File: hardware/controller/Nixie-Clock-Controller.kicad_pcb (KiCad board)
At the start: 2 copper layers, 228.6 x 69.8 mm, 67 parts, among them IC1 ESP32-DEVKITC-V4, IC2 74141, J1 9/12-35V DC in, J2 Nixies-Connector, J3 Input, J4 Output, J5 LEDs, J6 power_out, Q1 MPSA42, Q10 MPSA42, Q11 MPSA42, Q12 MPSA42, Q13 MPSA42, Q14 MPSA42, Q2 MPSA92, Q3 MPSA92, Q4 MPSA92, Q5 MPSA92, Q6 MPSA92, Q7 MPSA92, Q8 MPSA92, Q9 MPSA42, SW1 on/off, SW2 in voltage select, U1 L7805, U2 L7809, U3 NCH6300HV

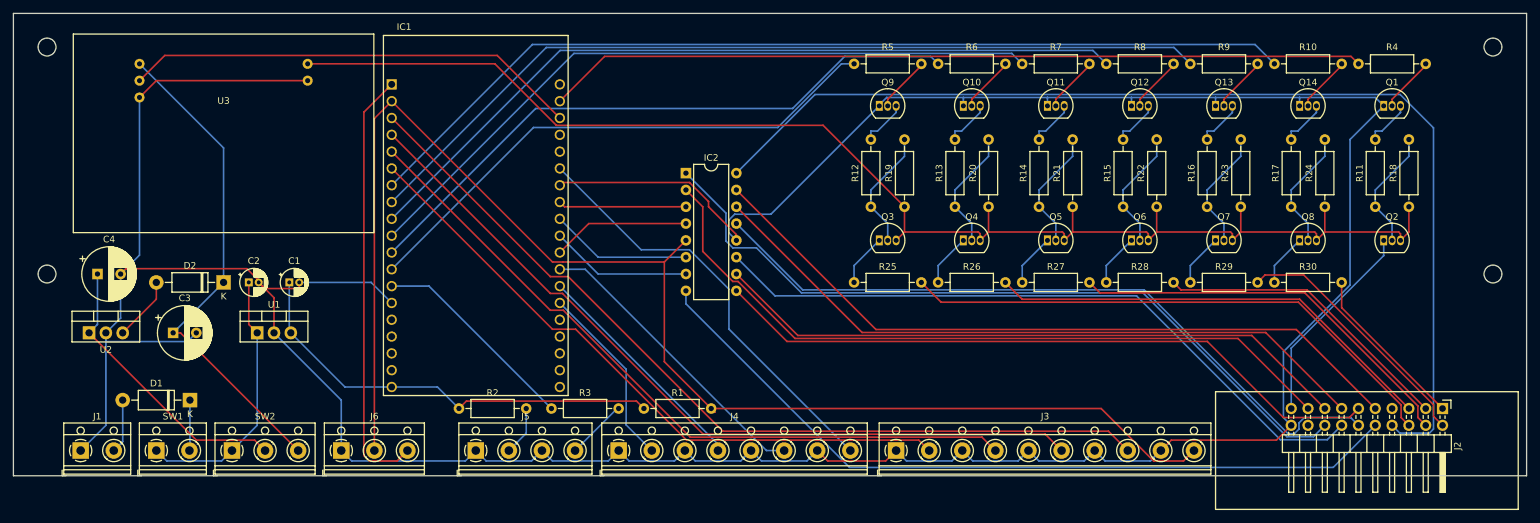
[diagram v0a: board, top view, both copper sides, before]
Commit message: Change Mountingholes to M3
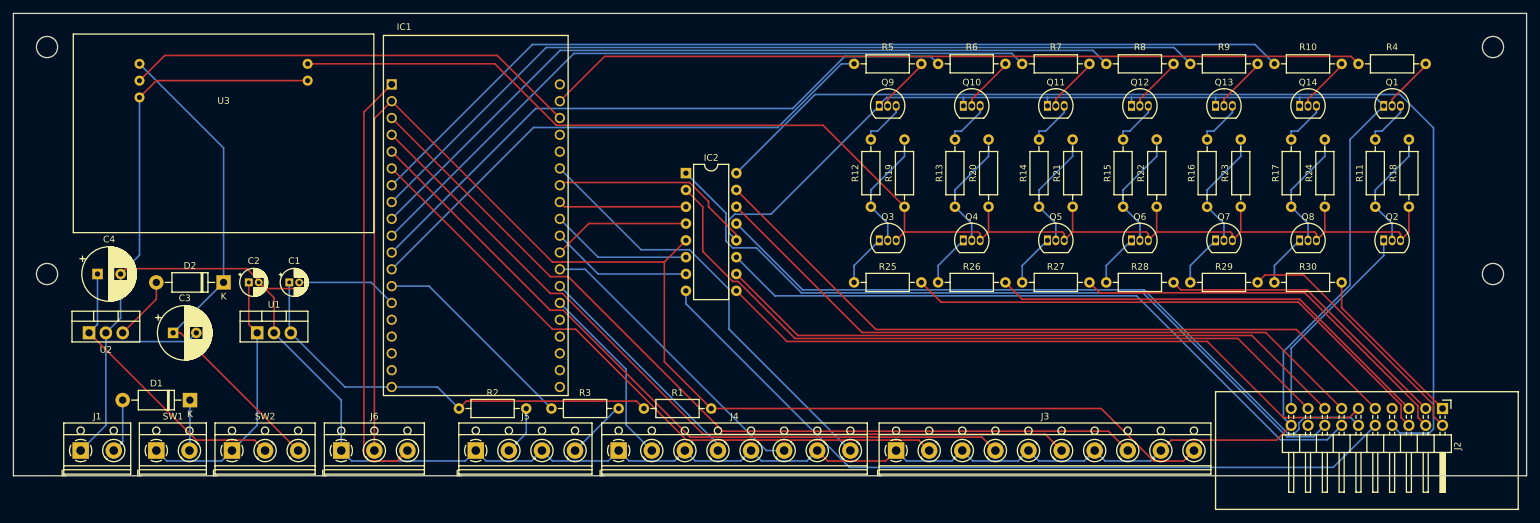
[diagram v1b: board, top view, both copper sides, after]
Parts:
- H1, H2, H3, H4: footprint MountingHole:MountingHole_2.7mm_M2.5 -> MountingHole:MountingHole_3.2mm_M3

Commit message: Fix wrong pin mapping on U3
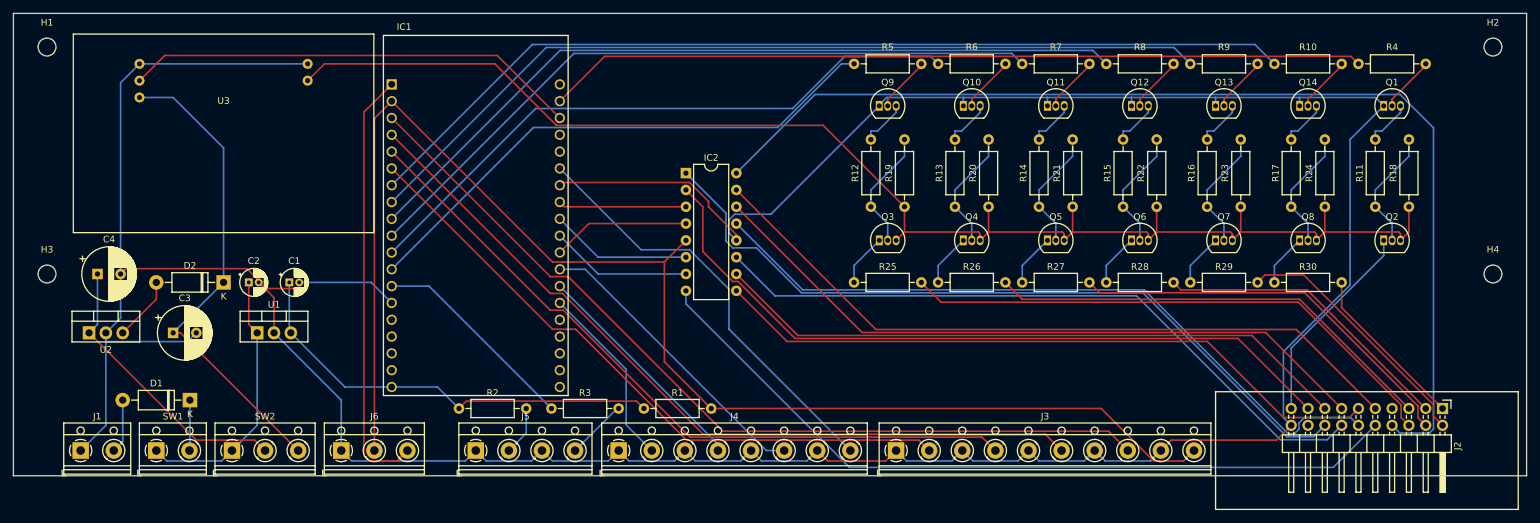
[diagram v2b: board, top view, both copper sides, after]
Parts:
- H1, H2, H3, H4: footprint MountingHole:MountingHole_3.2mm_M3 -> MountingHole:MountingHole_2.7mm_M2.5
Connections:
- IC1 pad 15: (no net) -> Net-(IC1-Pad15)
- IC1 pad 16: (no net) -> Net-(IC1-Pad16)
- IC1 pad 17: (no net) -> Net-(IC1-Pad17)
- IC1 pad 18: (no net) -> Net-(IC1-Pad18)
- IC1 pad 20: (no net) -> Net-(IC1-Pad20)
- IC1 pad 23: (no net) -> Net-(IC1-Pad23)
- IC1 pad 24: (no net) -> Net-(IC1-Pad24)
- IC1 pad 34: (no net) -> Net-(IC1-Pad34)
- IC1 pad 35: (no net) -> Net-(IC1-Pad35)
- IC1 pad 36: (no net) -> Net-(IC1-Pad36)
- IC1 pad 37: (no net) -> Net-(IC1-Pad37)
- IC1 pad 38: (no net) -> Net-(IC1-Pad38)
- J2 pad 18: (no net) -> Net-(J2-Pad18)
- J2 pad 7: (no net) -> Net-(J2-Pad7)
- U3 pad 1: Net-(C3-Pad1) -> GND
- U3 pad 3: GND -> Net-(C3-Pad1)
- U3 pad 4: Net-(Q2-Pad3) -> GND
- U3 pad 5: GND -> Net-(Q2-Pad3)
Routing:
- net GND: track 536.1 -> 540.1 mm
- net Net-(C3-Pad1): track 75.3 -> 73.2 mm
- net Net-(Q2-Pad3): track 213.6 -> 214.7 mm

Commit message: Move to Kicad 6
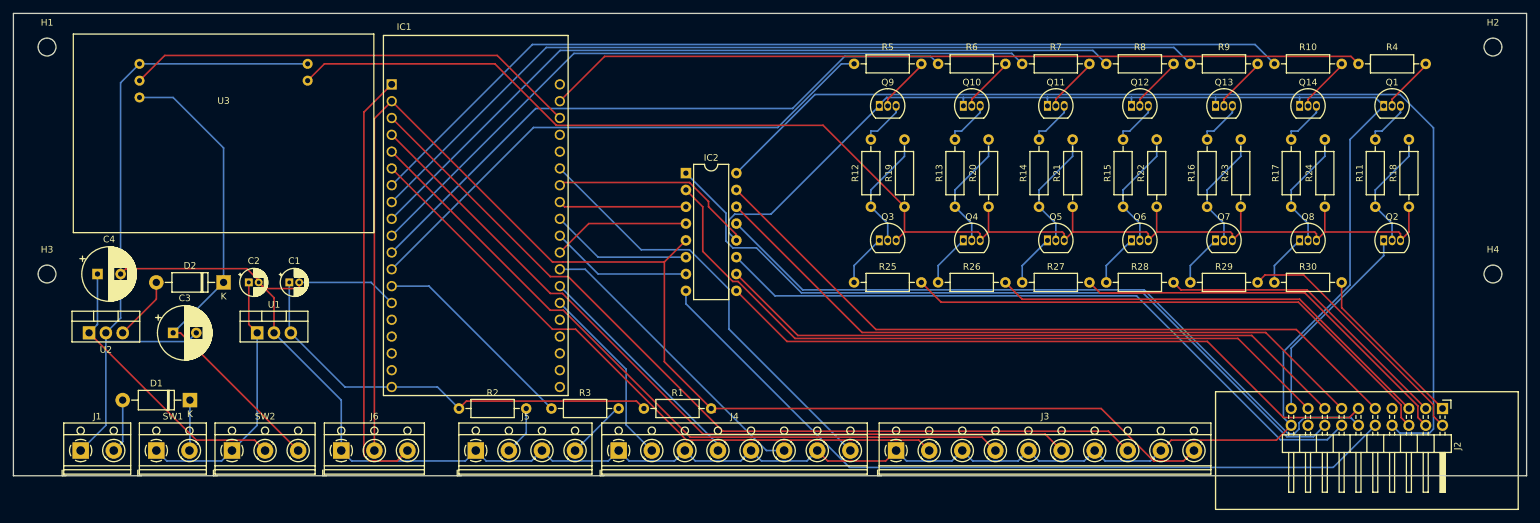
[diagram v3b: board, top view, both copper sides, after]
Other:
- net class Default removed

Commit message: Fix pin Layout again
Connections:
- IC1 pad 15: Net-(IC1-Pad15) -> unconnected-(IC1-Pad15)
- IC1 pad 16: Net-(IC1-Pad16) -> unconnected-(IC1-Pad16)
- IC1 pad 17: Net-(IC1-Pad17) -> unconnected-(IC1-Pad17)
- IC1 pad 18: Net-(IC1-Pad18) -> unconnected-(IC1-Pad18)
- IC1 pad 20: Net-(IC1-Pad20) -> unconnected-(IC1-Pad20)
- IC1 pad 23: Net-(IC1-Pad23) -> unconnected-(IC1-Pad23)
- IC1 pad 24: Net-(IC1-Pad24) -> unconnected-(IC1-Pad24)
- IC1 pad 34: Net-(IC1-Pad34) -> unconnected-(IC1-Pad34)
- IC1 pad 35: Net-(IC1-Pad35) -> unconnected-(IC1-Pad35)
- IC1 pad 36: Net-(IC1-Pad36) -> unconnected-(IC1-Pad36)
- IC1 pad 37: Net-(IC1-Pad37) -> unconnected-(IC1-Pad37)
- IC1 pad 38: Net-(IC1-Pad38) -> unconnected-(IC1-Pad38)
- J2 pad 18: Net-(J2-Pad18) -> unconnected-(J2-Pad18)
- J2 pad 7: Net-(J2-Pad7) -> unconnected-(J2-Pad7)

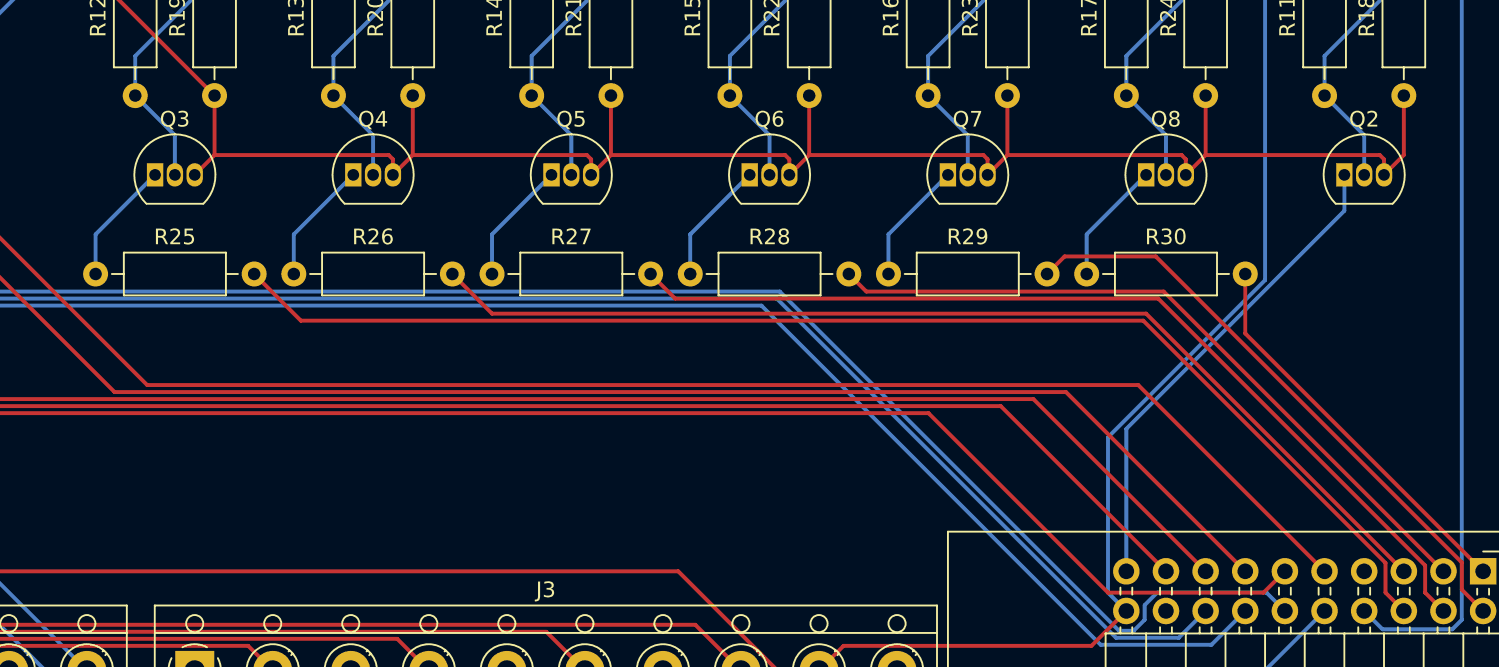
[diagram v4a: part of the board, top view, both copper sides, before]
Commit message: fix wrong transistor connections
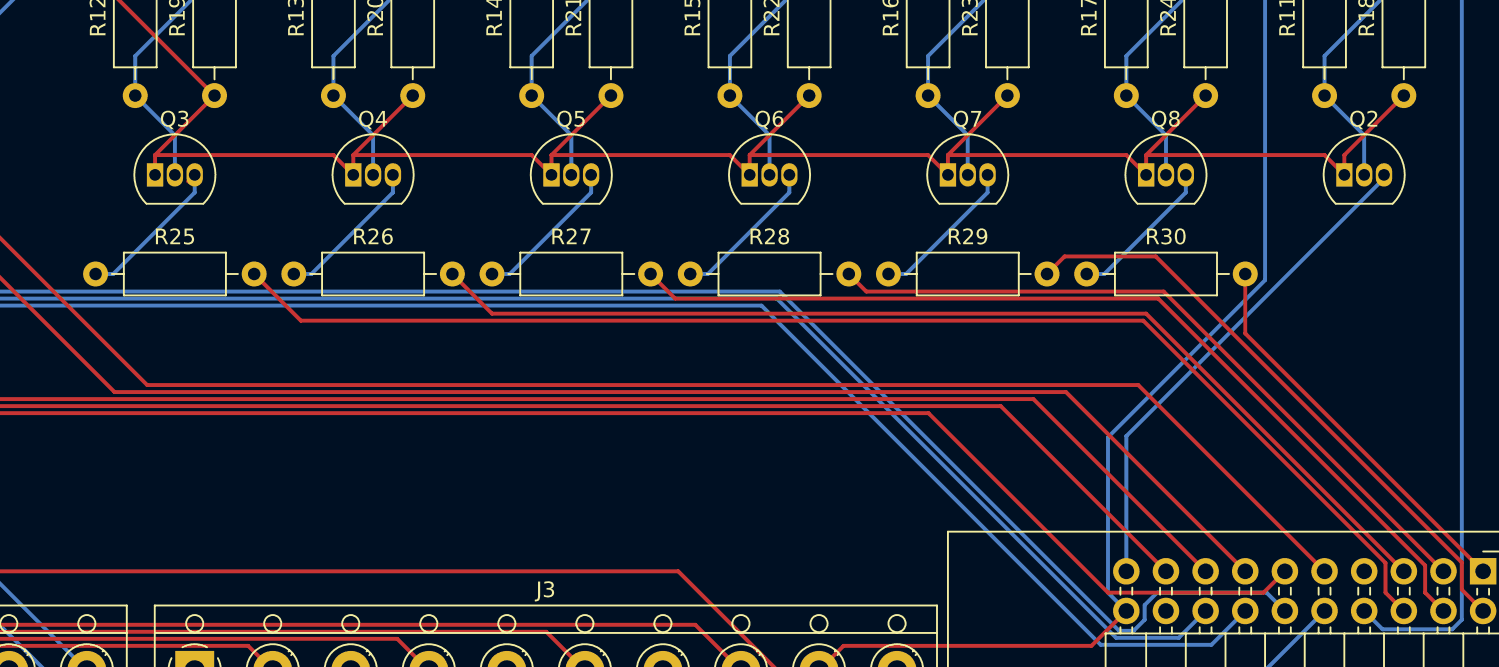
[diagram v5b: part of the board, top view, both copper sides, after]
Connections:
- Q2 pad 1: /da -> Net-(Q3-Pad1)
- Q2 pad 3: Net-(Q2-Pad3) -> /da
- Q3 pad 3: Net-(Q2-Pad3) -> Net-(R25-Pad1)
- Q4 pad 1: Net-(Q4-Pad1) -> Net-(Q3-Pad1)
- Q4 pad 3: Net-(Q2-Pad3) -> Net-(R26-Pad1)
- Q5 pad 1: Net-(Q5-Pad1) -> Net-(Q3-Pad1)
- Q5 pad 3: Net-(Q2-Pad3) -> Net-(Q5-Pad3)
- Q6 pad 1: Net-(Q6-Pad1) -> Net-(Q3-Pad1)
- Q6 pad 3: Net-(Q2-Pad3) -> Net-(Q6-Pad3)
- Q7 pad 1: Net-(Q7-Pad1) -> Net-(Q3-Pad1)
- Q7 pad 3: Net-(Q2-Pad3) -> Net-(Q7-Pad3)
- Q8 pad 1: Net-(Q8-Pad1) -> Net-(Q3-Pad1)
- Q8 pad 3: Net-(Q2-Pad3) -> Net-(Q8-Pad3)
- R18 pad 1: Net-(Q2-Pad3) -> Net-(Q3-Pad1)
- R19 pad 1: Net-(Q2-Pad3) -> Net-(Q3-Pad1)
- R20 pad 1: Net-(Q2-Pad3) -> Net-(Q3-Pad1)
- R21 pad 1: Net-(Q2-Pad3) -> Net-(Q3-Pad1)
- R22 pad 1: Net-(Q2-Pad3) -> Net-(Q3-Pad1)
- R23 pad 1: Net-(Q2-Pad3) -> Net-(Q3-Pad1)
- R24 pad 1: Net-(Q2-Pad3) -> Net-(Q3-Pad1)
- R25 pad 1: Net-(Q3-Pad1) -> Net-(R25-Pad1)
- R26 pad 1: Net-(Q4-Pad1) -> Net-(R26-Pad1)
- R27 pad 1: Net-(Q5-Pad1) -> Net-(Q5-Pad3)
- R28 pad 1: Net-(Q6-Pad1) -> Net-(Q6-Pad3)
- R29 pad 1: Net-(Q7-Pad1) -> Net-(Q7-Pad3)
- R30 pad 1: Net-(Q8-Pad1) -> Net-(Q8-Pad3)
- U3 pad 5: Net-(Q2-Pad3) -> Net-(Q3-Pad1)
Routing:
- net Net-(Q3-Pad1): track 7.93 -> 226.1 mm
- net Net-(Q2-Pad3): track 214.7 -> 0.00 mm
- net Net-(R25-Pad1): track 0.00 -> 10.2 mm
- net Net-(R26-Pad1): track 0.00 -> 9.64 mm
- net Net-(Q8-Pad3): track 0.00 -> 9.64 mm
- net Net-(Q6-Pad3): track 0.00 -> 9.64 mm
- net Net-(Q5-Pad3): track 0.00 -> 9.64 mm
- net Net-(Q7-Pad3): track 0.00 -> 9.64 mm
- net Net-(Q8-Pad1): track 7.93 -> 0.00 mm
- net Net-(Q7-Pad1): track 7.93 -> 0.00 mm
- net Net-(Q6-Pad1): track 7.93 -> 0.00 mm
- net Net-(Q5-Pad1): track 7.93 -> 0.00 mm
- net Net-(Q4-Pad1): track 7.93 -> 0.00 mm
- net /da: track 31.2 -> 32.2 mm

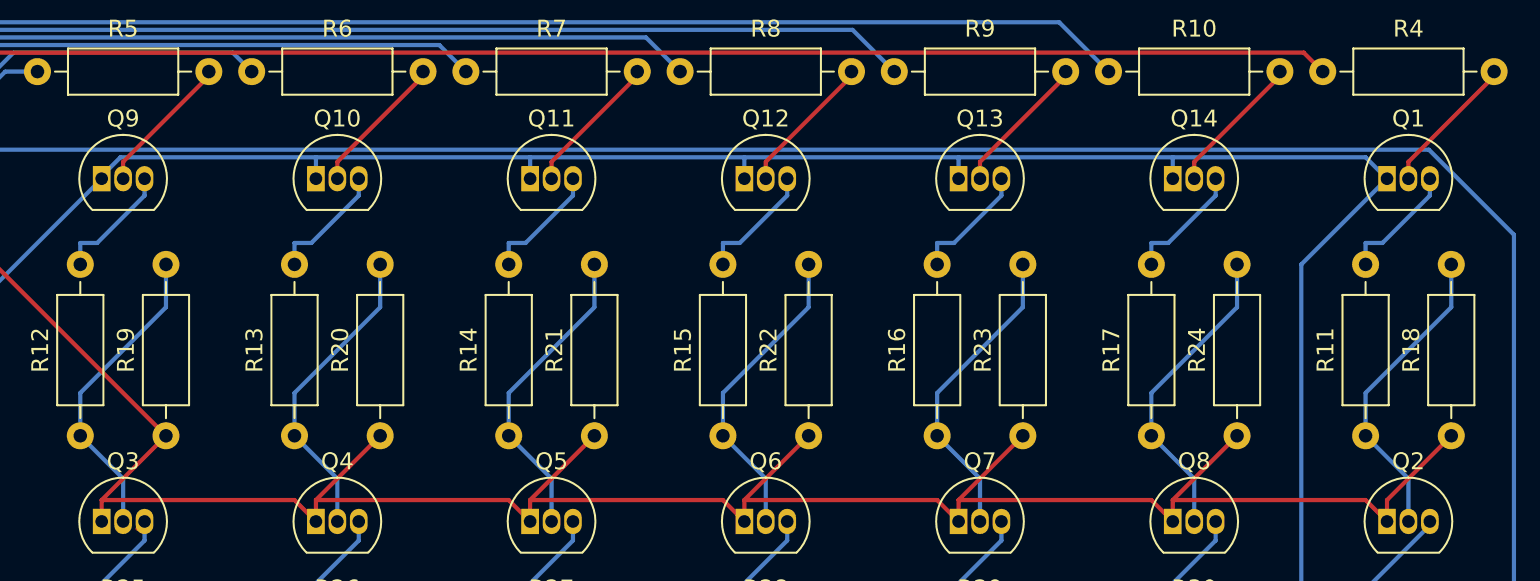
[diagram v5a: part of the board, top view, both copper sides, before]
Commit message: Improve transistor numbering
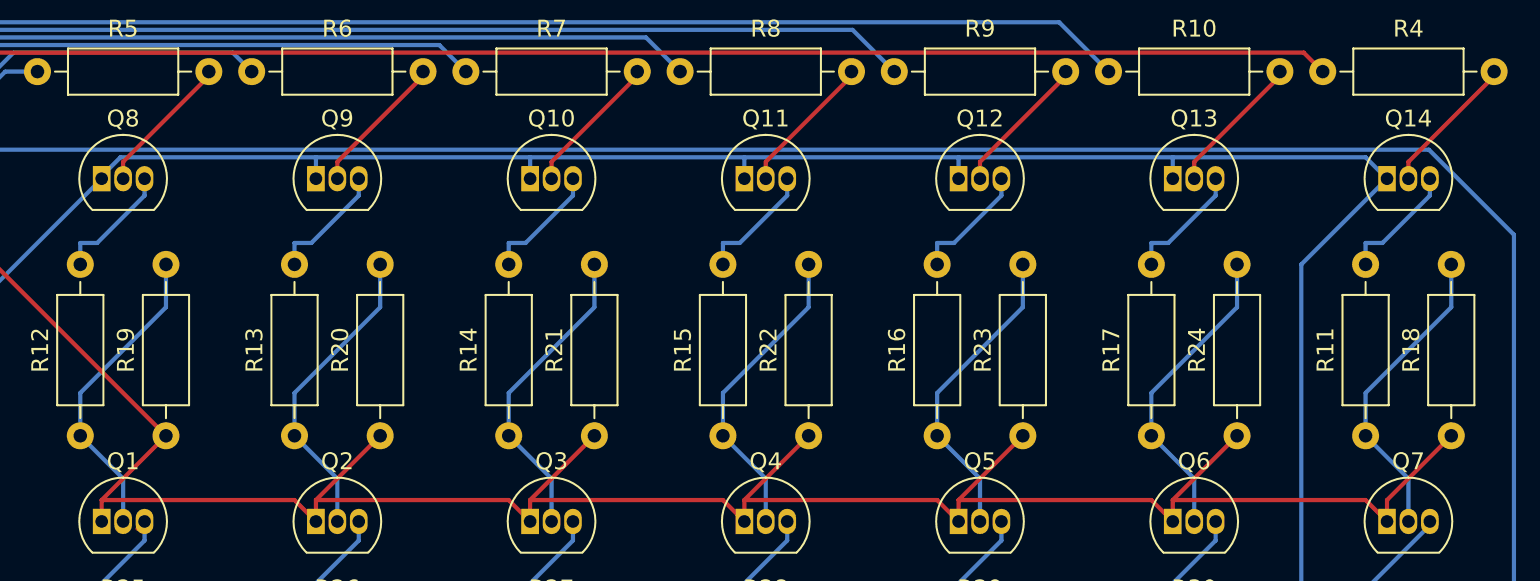
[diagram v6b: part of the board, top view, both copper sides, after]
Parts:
- renumbered Q3 to Q1, Q11 to Q10, Q12 to Q11, Q13 to Q12, Q14 to Q13, Q1 to Q14, Q4 to Q2, Q5 to Q3, Q6 to Q4, Q7 to Q5, Q8 to Q6, Q2 to Q7, Q9 to Q8, Q10 to Q9

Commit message: Add version text
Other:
- board text added: "Nixie-Clock-Controller v1.1 (16.01.2022) konradmoesch"
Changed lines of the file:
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@@
   (gr_line (start 13.97 83.82) (end 13.97 13.97) (layer "Edge.Cuts") (width 0.05))
   (gr_line (start 242.57 83.82) (end 13.97 83.82) (layer "Edge.Cuts") (width 0.05))
+  (gr_text "Nixie-Clock-Controller\nv1.1 (16.01.2022)\nkonradmoesch" (at 106.3 25.4) (layer "F.SilkS")
+    (effects (font (size 1.5 1.5) (thickness 0.3)) (justify left))
+  )
   (segment (start 116.11 39.515) (end 96.935 39.515) (width 0.25) (layer "F.Cu") (net 1))
   (segment (start 123.19 47.385) (end 118.985 43.18) (width 0.25) (layer "F.Cu") (net 1))
